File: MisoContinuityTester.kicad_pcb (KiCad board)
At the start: 2 copper layers, 150 x 66 mm, 21 parts, among them J10 OUTPUT, J11 OUTPUT, J12 TYPE1, J13 TYPE2, J3 POWER SWITCH, J4 INPUT, J5 INPUT, J6 FAIL, J7 PASS, J8 POWER 5V-12V, J9 START

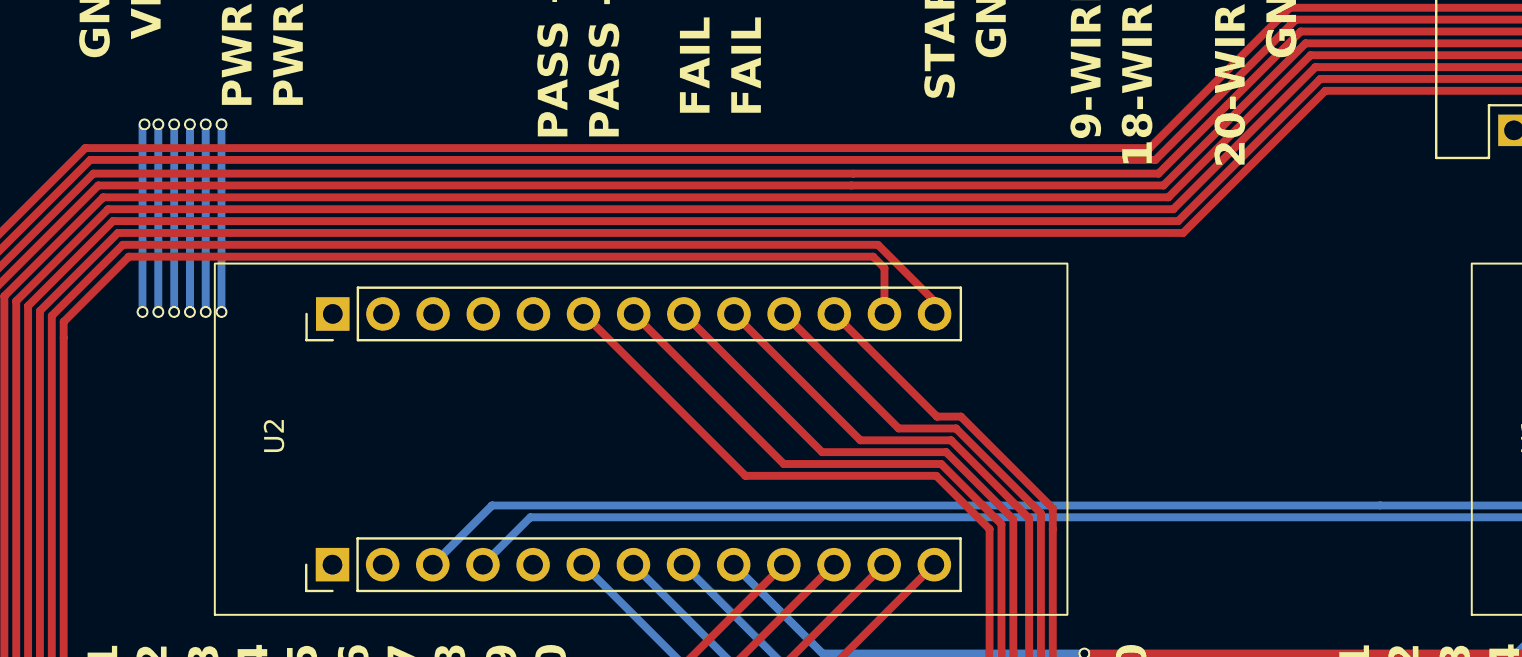
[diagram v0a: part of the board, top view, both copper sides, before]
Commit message: added lables Expander 1 and Expander 2 so we can tell each expanders i/o pins a part
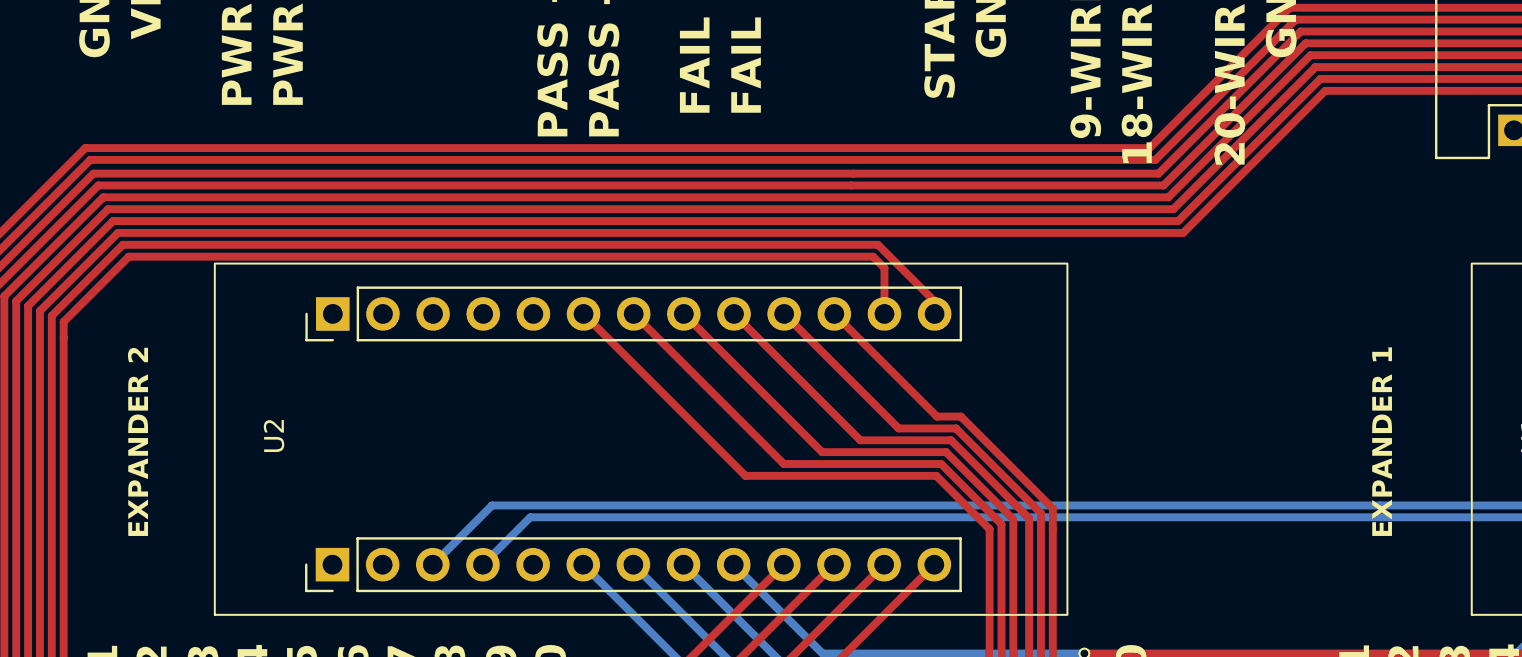
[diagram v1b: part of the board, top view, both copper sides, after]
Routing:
- net +5V: track 57.0 -> 0.00 mm, vias 12 -> 0
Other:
- board text added: "EXPANDER 1"
- board text added: "EXPANDER 2"
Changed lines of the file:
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@@
 			(psa4output no)
 			(plot_black_and_white yes)
-			(plotinvisibletext no)
 			(sketchpadsonfab no)
 			(plotpadnumbers no)
@@
 		)
 	)
+	(gr_text "EXPANDER 2"
+		(at 70.5 102.67 90)
+		(layer "F.SilkS")
+		(effects
+			(font
+				(size 1 1)
+				(thickness 0.2)
+				(bold yes)
+			)
+			(justify left bottom)
+		)
+	)
 	(gr_text "B14"
 		(at 76.6 112.4 90)
@@
 		)
 	)
+	(gr_text "EXPANDER 1"
+		(at 133.5 102.67 90)
+		(layer "F.SilkS")
+		(effects
+			(font
+				(size 1 1)
+				(thickness 0.2)
+				(bold yes)
+			)
+			(justify left bottom)
+		)
+	)
 	(gr_text "PWR A"
 		(at 75.8 80.9 90)
@@
 		(net 2)
 	)
-	(via
-		(at 71.7 81.7)
-		(size 0.6)
-		(drill 0.4)
-		(layers "F.Cu" "B.Cu")
-		(free yes)
-		(net 3)
-	)
-	(via
-		(at 73.3 81.7)
-		(size 0.6)
-		(drill 0.4)
-		(layers "F.Cu" "B.Cu")
-		(free yes)
-		(net 3)
-	)
-	(via
-		(at 70.9 91.2)
-		(size 0.6)
-		(drill 0.4)
-		(layers "F.Cu" "B.Cu")
-		(net 3)
-	)
-	(via
-		(at 70.1 91.2)
-		(size 0.6)
-		(drill 0.4)
-		(layers "F.Cu" "B.Cu")
-		(net 3)
-	)
-	(via
-		(at 74.1 91.2)
-		(size 0.6)
-		(drill 0.4)
-		(layers "F.Cu" "B.Cu")
-		(net 3)
-	)
-	(via
-		(at 74.1 81.7)
-		(size 0.6)
-		(drill 0.4)
-		(layers "F.Cu" "B.Cu")
-		(free yes)
-		(net 3)
-	)
-	(via
-		(at 72.5 81.7)
-		(size 0.6)
-		(drill 0.4)
-		(layers "F.Cu" "B.Cu")
-		(free yes)
-		(net 3)
-	)
-	(via
-		(at 73.3 91.2)
-		(size 0.6)
-		(drill 0.4)
-		(layers "F.Cu" "B.Cu")
-		(net 3)
-	)
-	(via
-		(at 71.7 91.2)
-		(size 0.6)
-		(drill 0.4)
-		(layers "F.Cu" "B.Cu")
-		(net 3)
-	)
-	(via
-		(at 70.2 81.7)
-		(size 0.6)
-		(drill 0.4)
-		(layers "F.Cu" "B.Cu")
-		(free yes)
-		(net 3)
-	)
-	(via
-		(at 72.5 91.2)
-		(size 0.6)
-		(drill 0.4)
-		(layers "F.Cu" "B.Cu")
-		(net 3)
-	)
-	(via
-		(at 70.9 81.7)
-		(size 0.6)
-		(drill 0.4)
-		(layers "F.Cu" "B.Cu")
-		(free yes)
-		(net 3)
-	)
-	(segment
-		(start 71.7 81.7)
-		(end 71.7 91.2)
-		(width 0.4)
-		(layer "B.Cu")
-		(net 3)
-	)
-	(segment
-		(start 70.9 81.7)
-		(end 70.9 91.2)
-		(width 0.4)
-		(layer "B.Cu")
-		(net 3)
-	)
-	(segment
-		(start 74.1 81.7)
-		(end 74.1 91.2)
-		(width 0.4)
-		(layer "B.Cu")
-		(net 3)
-	)
-	(segment
-		(start 73.3 81.7)
-		(end 73.3 91.2)
-		(width 0.4)
-		(layer "B.Cu")
-		(net 3)
-	)
-	(segment
-		(start 70.1 81.8)
-		(end 70.1 91.2)
-		(width 0.4)
-		(layer "B.Cu")
-		(net 3)
-	)
-	(segment
-		(start 70.2 81.7)
-		(end 70.1 81.8)
-		(width 0.4)
-		(layer "B.Cu")
-		(net 3)
-	)
-	(segment
-		(start 72.5 81.7)
-		(end 72.5 91.2)
-		(width 0.4)
-		(layer "B.Cu")
-		(net 3)
-	)
 	(segment
